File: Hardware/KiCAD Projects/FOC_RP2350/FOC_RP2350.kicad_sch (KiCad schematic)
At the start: 0 parts

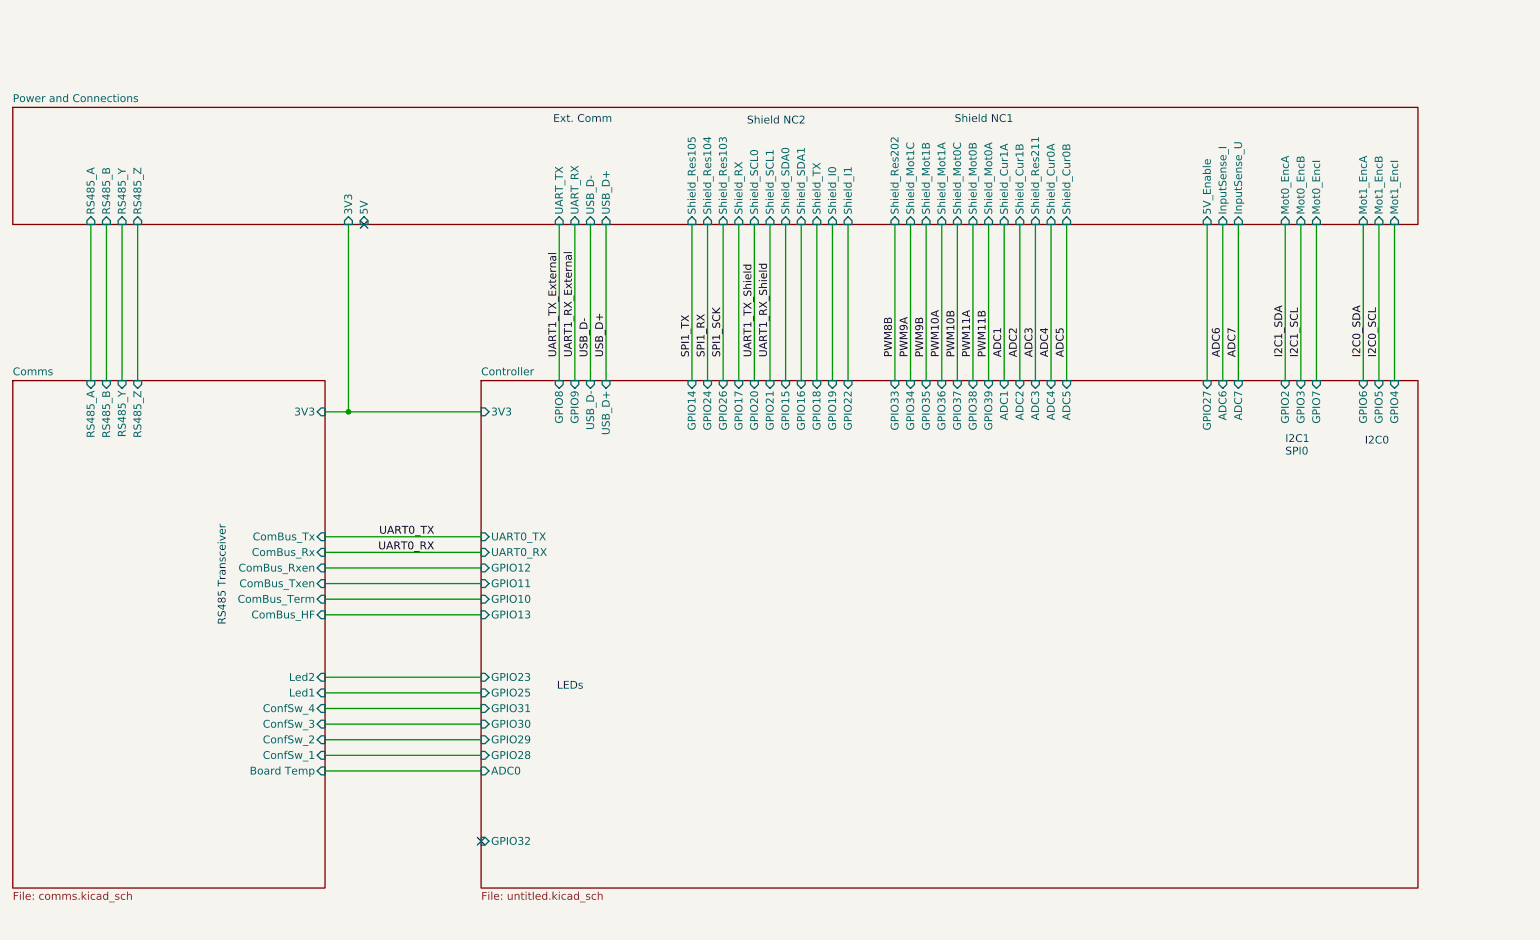
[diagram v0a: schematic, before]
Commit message: Hardware update
- Removed 5V net as it is not really needed for typical SimpleFOC encoders. This reduces part cost a lot.
- Fixed SPI pin assignment
- Exposed another GPIO pin in place of the +5V pin
- Boards changed to transfer power via the standoff pads instead of a solder connection
- Moved accelerometer to the controller board
- Resistance changes to reduce BOM
- Replaced encoder connection with JST-XH
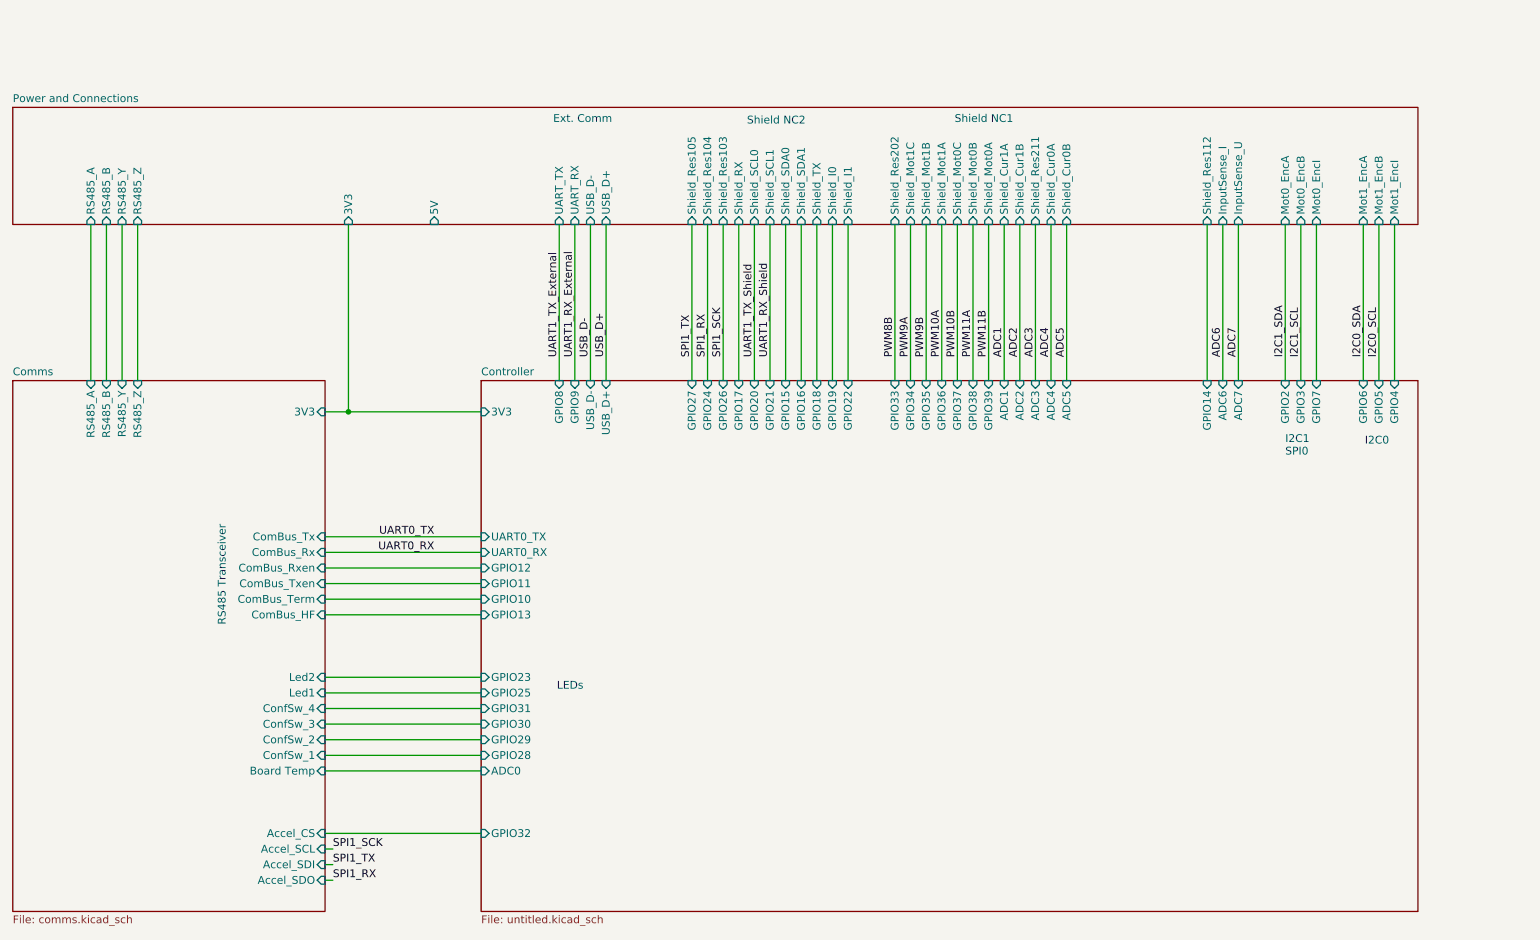
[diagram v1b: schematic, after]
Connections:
- no-connect marks 2 -> 0
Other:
- sheet Comms ports: added Accel_CS, Accel_SCL, Accel_SDI, Accel_SDO; removed none
- sheet Power and Connections ports: added Shield_Res112; removed 5V_Enable
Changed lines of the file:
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@@
 		(color 0 0 0 0)
 	)
-	(no_connect
-		(at 109.22 146.05)
-	)
-	(no_connect
-		(at 90.17 45.72)
-	)
 	(wire
 		(pts
@@
 	(wire
 		(pts
+			(xy 83.82 144.78) (xy 109.22 144.78)
+		)
+		(stroke
+			(width 0)
+			(type default)
+		)
+	)
+	(wire
+		(pts
 			(xy 124.46 45.72) (xy 124.46 71.12)
 		)
@@
 	(wire
 		(pts
+			(xy 83.82 149.86) (xy 85.09 149.86)
+		)
+		(stroke
+			(width 0)
+			(type default)
+		)
+	)
+	(wire
+		(pts
 			(xy 232.41 45.72) (xy 232.41 71.12)
 		)
@@
 	(wire
 		(pts
+			(xy 83.82 147.32) (xy 85.09 147.32)
+		)
+		(stroke
+			(width 0)
+			(type default)
+		)
+	)
+	(wire
+		(pts
 			(xy 83.82 124.46) (xy 109.22 124.46)
 		)
@@
 		(pts
 			(xy 255.27 45.72) (xy 255.27 71.12)
+		)
+		(stroke
+			(width 0)
+			(type default)
+		)
+	)
+	(wire
+		(pts
+			(xy 83.82 152.4) (xy 85.09 152.4)
 		)
 		(stroke
@@
 		)
 	)
+	(label "SPI1_TX"
+		(at 85.09 149.86 0)
+		(effects
+			(font
+				(size 1.27 1.27)
+			)
+			(justify left bottom)
+		)
+	)
 	(label "SPI1_SCK"
 		(at 148.59 67.31 90)
@@
 		)
 	)
+	(label "SPI1_SCK"
+		(at 85.09 147.32 0)
+		(effects
+			(font
+				(size 1.27 1.27)
+			)
+			(justify left bottom)
+		)
+	)
 	(label "PWM9A"
 		(at 179.07 67.31 90)
@@
 		)
 	)
+	(label "SPI1_RX"
+		(at 85.09 152.4 0)
+		(effects
+			(font
+				(size 1.27 1.27)
+			)
+			(justify left bottom)
+		)
+	)
 	(label "UART1_TX_External"
 		(at 121.92 67.31 90)
@@
 	(sheet
 		(at 109.22 71.12)
-		(size 152.4 82.55)
+		(size 152.4 86.36)
 		(exclude_from_sim no)
 		(in_bom yes)
@@
 		)
 		(property "Sheetfile" "untitled.kicad_sch"
-			(at 109.22 154.2546 0)
+			(at 109.22 158.0646 0)
 			(show_name no)
 			(do_not_autoplace no)
@@
 		)
 		(pin "GPIO32" input
-			(at 109.22 146.05 180)
+			(at 109.22 144.78 180)
 			(effects
 				(font
@@
 			)
 		)
-		(pin "GPIO14" input
-			(at 143.51 71.12 90)
-			(effects
-				(font
-					(size 1.27 1.27)
-				)
-				(justify right)
-			)
-		)
-		(pin "GPIO27" input
-			(at 227.33 71.12 90)
-			(effects
-				(font
-					(size 1.27 1.27)
-				)
-				(justify right)
-			)
-		)
 		(pin "GPIO15" input
 			(at 158.75 71.12 90)
@@
 		(pin "GPIO7" input
 			(at 245.11 71.12 90)
+			(effects
+				(font
+					(size 1.27 1.27)
+				)
+				(justify right)
+			)
+		)
+		(pin "GPIO14" input
+			(at 227.33 71.12 90)
+			(effects
+				(font
+					(size 1.27 1.27)
+				)
+				(justify right)
+			)
+		)
+		(pin "GPIO27" input
+			(at 143.51 71.12 90)
 			(effects
 				(font
@@
 			)
 		)
-		(pin "5V_Enable" input
-			(at 227.33 45.72 270)
-			(effects
-				(font
-					(size 1.27 1.27)
-				)
-				(justify left)
-			)
-		)
 		(pin "InputSense_I" input
 			(at 229.87 45.72 270)
@@
 			)
 		)
-		(pin "5V" input
-			(at 90.17 45.72 270)
-			(effects
-				(font
-					(size 1.27 1.27)
-				)
-				(justify left)
-			)
-		)
 		(pin "Shield_Res103" input
 			(at 148.59 45.72 270)
@@
 		(pin "Shield_Res104" input
 			(at 146.05 45.72 270)
+			(effects
+				(font
+					(size 1.27 1.27)
+				)
+				(justify left)
+			)
+		)
+		(pin "Shield_Res112" input
+			(at 227.33 45.72 270)
+			(effects
+				(font
+					(size 1.27 1.27)
+				)
+				(justify left)
+			)
+		)
+		(pin "5V" input
+			(at 101.6 45.72 270)
 			(effects
 				(font
@@
 	(sheet
 		(at 33.02 71.12)
-		(size 50.8 82.55)
+		(size 50.8 86.36)
 		(exclude_from_sim no)
 		(in_bom yes)
@@
 		)
 		(property "Sheetfile" "comms.kicad_sch"
-			(at 33.02 154.2546 0)
+			(at 33.02 158.0646 0)
 			(show_name no)
 			(do_not_autoplace no)
@@
 			(effects
 				(font
+					(size 1.27 1.27)
+				)
+				(justify right)
+			)
+		)
+		(pin "Accel_CS" input
+			(at 83.82 144.78 0)
+			(effects
+				(font
+					(size 1.27 1.27)
+				)
+				(justify right)
+			)
+		)
+		(pin "Accel_SCL" input
+			(at 83.82 147.32 0)
+			(effects
+				(font
+					(size 1.27 1.27)
+				)
+				(justify right)
+			)
+		)
+		(pin "Accel_SDI" input
+			(at 83.82 149.86 0)
+			(effects
+				(font
+					(size 1.27 1.27)
+				)
+				(justify right)
+			)
+		)
+		(pin "Accel_SDO" input
+			(at 83.82 152.4 0)
+			(effects
+				(font

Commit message: Driver redesign to allow 8323H and 8323S
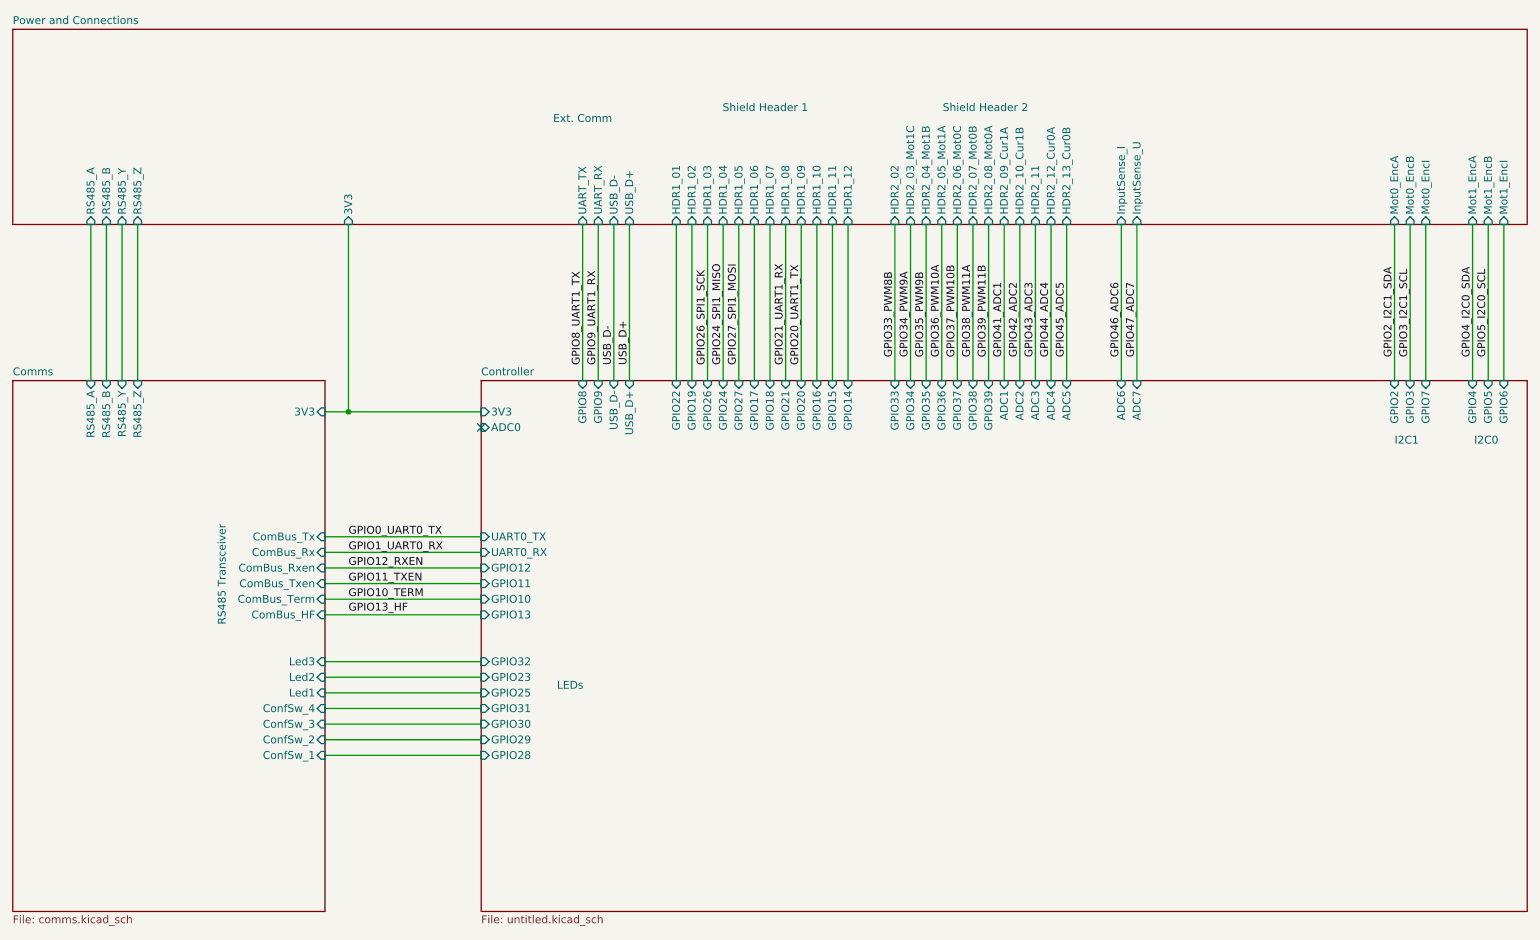
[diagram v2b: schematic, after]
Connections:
- no-connect marks 0 -> 1
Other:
- sheet Comms ports: added Led3; removed Accel_CS, Accel_SCL, Accel_SDI, Accel_SDO, Board Temp
- sheet Power and Connections ports: added HDR1_01, HDR1_02, HDR1_03, HDR1_04, HDR1_05, HDR1_06, HDR1_07, HDR1_08, HDR1_09, HDR1_10, HDR1_11, HDR1_12, HDR2_02, HDR2_03_Mot1C, HDR2_04_Mot1B, HDR2_05_Mot1A, HDR2_06_Mot0C, HDR2_07_Mot0B, HDR2_08_Mot0A, HDR2_09_Cur1A, HDR2_10_Cur1B, HDR2_11, HDR2_12_Cur0A, HDR2_13_Cur0B; removed 5V, Shield_Cur0A, Shield_Cur0B, Shield_Cur1A, Shield_Cur1B, Shield_I0, Shield_I1, Shield_Mot0A, Shield_Mot0B, Shield_Mot0C, Shield_Mot1A, Shield_Mot1B, Shield_Mot1C, Shield_RX, Shield_Res103, Shield_Res104, Shield_Res105, Shield_Res112, Shield_Res202, Shield_Res211, Shield_SCL0, Shield_SCL1, Shield_SDA0, Shield_SDA1, Shield_TX
- note added: "I2C1"
- note added: "Shield Header 1"
- note added: "Shield Header 2"
- note removed: "I2C1 SPI0"
- note removed: "Shield NC1"
- note removed: "Shield NC2"
